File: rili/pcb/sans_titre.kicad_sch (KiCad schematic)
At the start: 1 part, among them U1 ESP32P4_QFN104

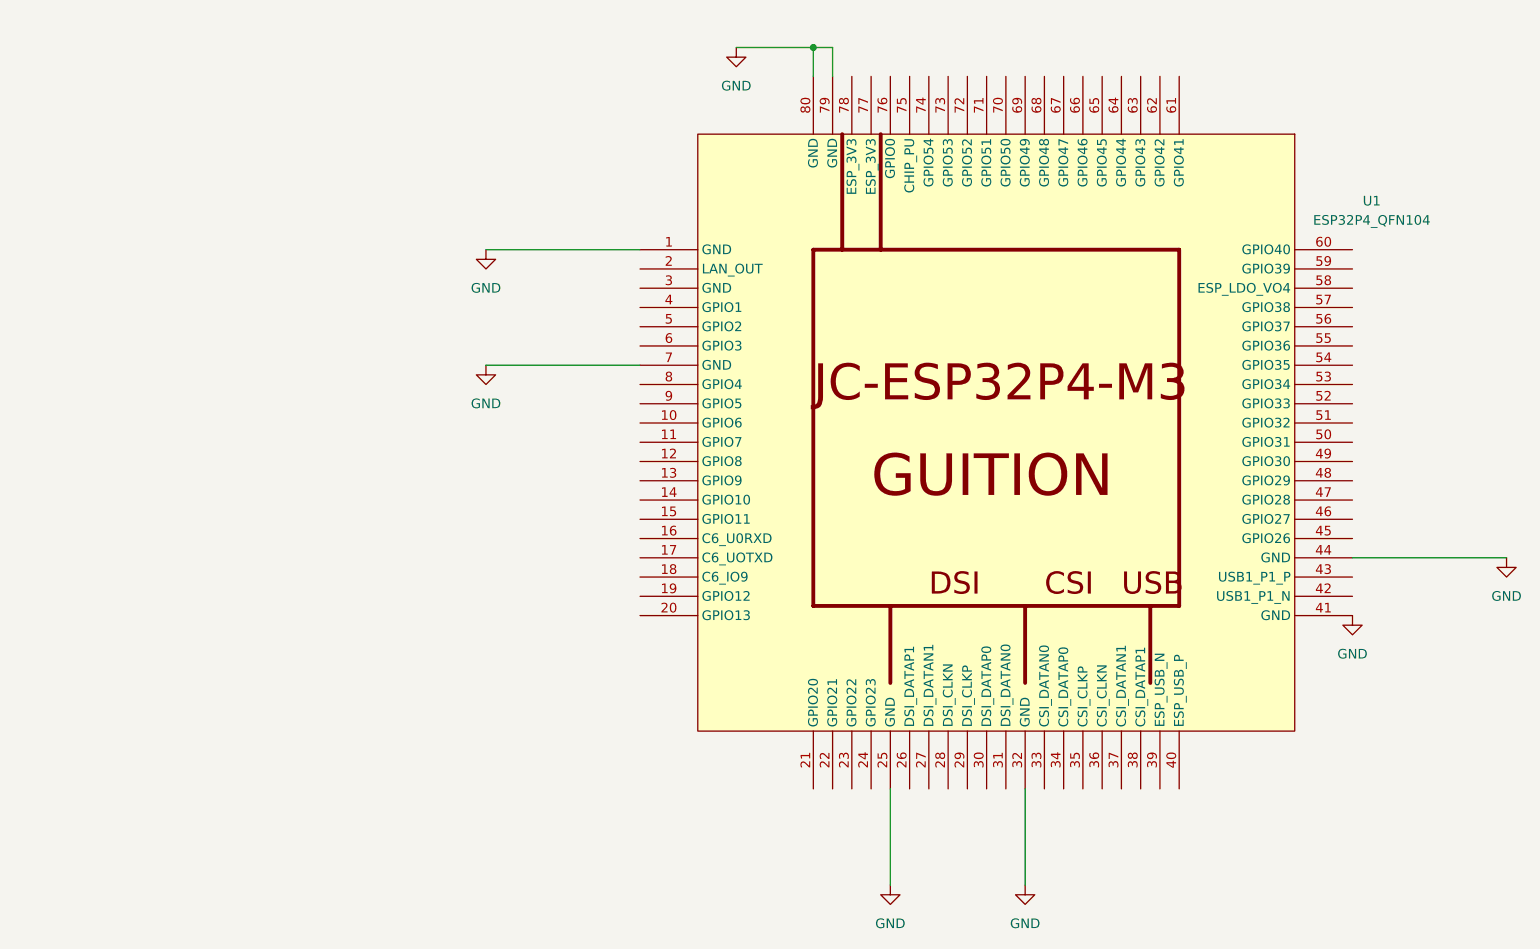
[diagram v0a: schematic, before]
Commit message: WIP schéma v2 Niphargus + rename projet rili → niphar
Grosse session schéma (binôme Mae/Claude) :
- Panneau 2 moitiés : matrice droite miroir, nets séparés (col*_d/row*_d)
- Feuille s3 : ESP32-S3-WROOM-1, matrice 11 GPIO RTC, nRF24 (SPI + 100R),
  J_PROG 6 pins (ESP-Prog), USB_DP/DM, TRRS J6 protégé (SRV05-4 shunt,
  100R série, load switch poignée de main 5V)
- Feuille bat : chaîne 16340 complète — DW01A+FS8205, TP4056 500mA,
  load-sharing AO3407, MCP1700, jauge VBAT_SENSE (validée par netlist)
- Feuille usb : USB-C 16P + CC 5k1 + USBLC6, hub CH334R (S3+P4, mode
  sans crystal, LDO interne isolé du rail 3V3, RESET# pull-up)
- Feuille P4 (coffre, en cours) + Matrix ; hiérarchie intégrée à la racine
- Ménage : fossiles corne-cherry supprimés (rescue.lib conservée, encore
  référencée) ; symbole FS8205 créé ; scripts/mirror_panel.py archivé
- Rename : projet KiCad rili.* → niphar.* (produit « Niphargus »),
  kicad-check.sh et CLAUDE.md retargetés

ERC : 87 erreurs restantes = chantier en cours (pins P4 en attente,
PWR_FLAG, GPIO libres à flagger) — push en connaissance de cause (--no-verify),
baselines à re-référencer quand le schéma sera complet.

Co-Authored-By: Claude Fable 5 <noreply@anthropic.com>
Claude-Session: https://claude.ai/code/session_01GfX5RmekmQi78Dm37qsT4Z
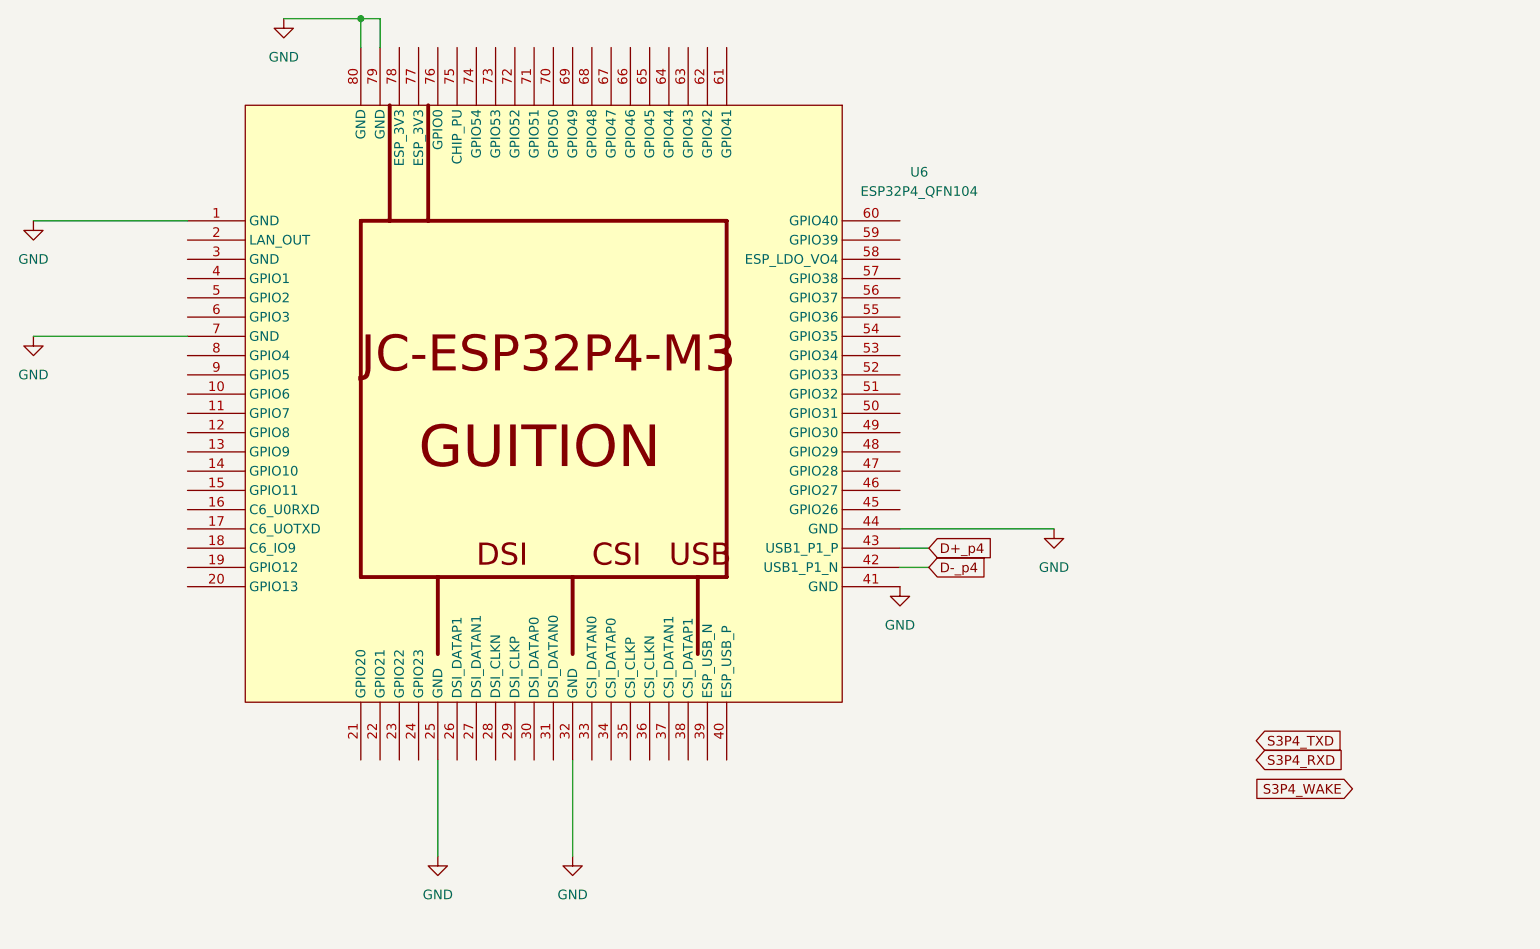
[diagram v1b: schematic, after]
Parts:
- renumbered U1 to U6
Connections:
- net D-_p4: now reaches U6.42 (USB1_P1_N)
- net D+_p4: now reaches U6.43 (USB1_P1_P)
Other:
- moved on the sheet: U6
